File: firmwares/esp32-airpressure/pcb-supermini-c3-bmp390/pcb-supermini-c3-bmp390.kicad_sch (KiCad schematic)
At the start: 11 parts, among them J1 JST GH 4_Socket, U1 ESP32-C3_SUPERMINI_SMD, U2 BMP390 MODULE, U3 CAN transciever

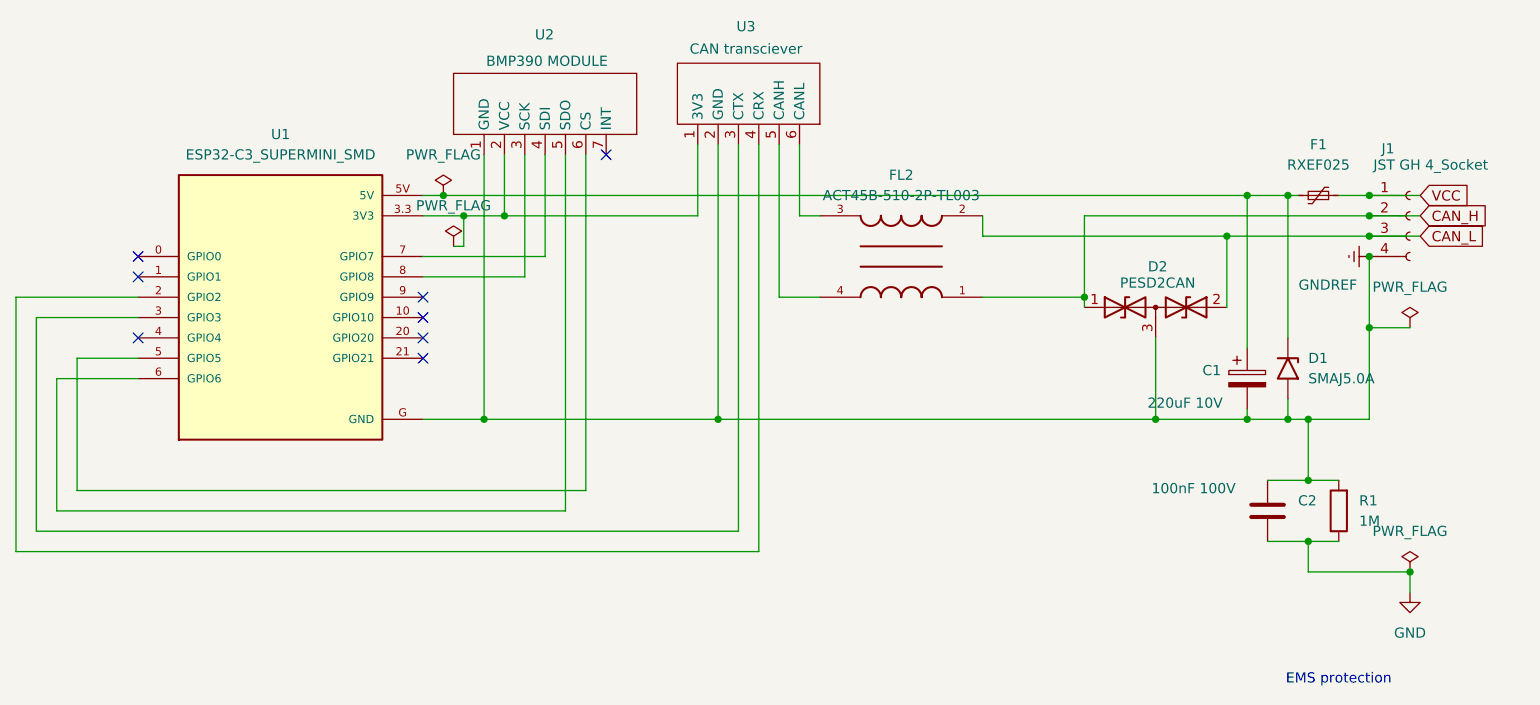
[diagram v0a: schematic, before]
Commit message: refactor: update PCB to be on 2 layers
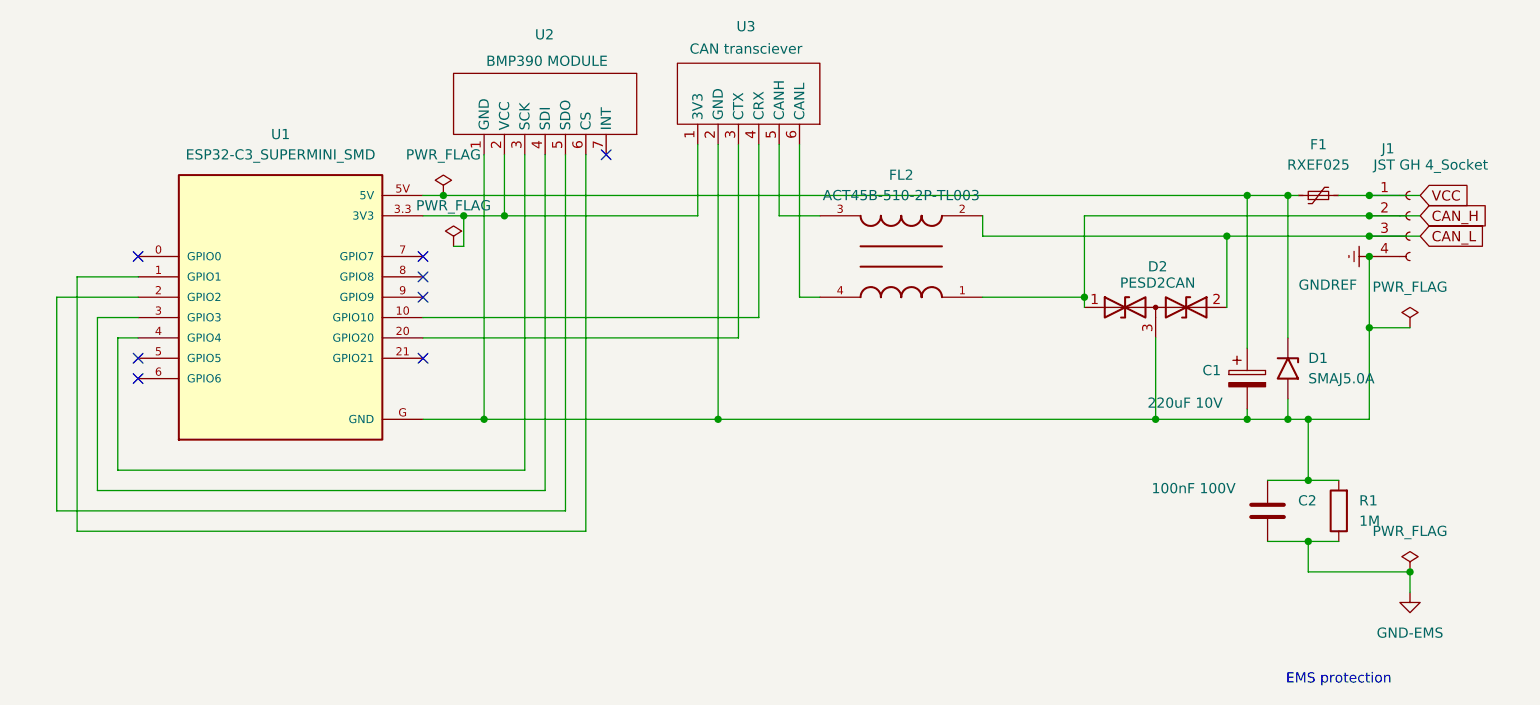
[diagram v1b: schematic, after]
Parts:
- J1: footprint Connector_JST:JST_GH_BM04B-GHS-TBT_1x04-1MP_P1.25mm_Vertical -> Connector_JST:JST_GH_SM04B-GHS-TB_1x04-1MP_P1.25mm_Horizontal
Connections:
- net at U1.1 (GPIO1): now also U2.6 (CS)
- net at U1.10 (GPIO10): now also U3.4 (CRX)
- net at U1.2 (GPIO2): now also U2.5 (SDO); no longer U3.4 (CRX)
- net at U1.20 (GPIO20): now also U3.3 (CTX)
- net at U1.3 (GPIO3): now also U2.4 (SDI); no longer U3.3 (CTX)
- net at U1.4 (GPIO4): now also U2.3 (SCK)
- net at U1.5 (GPIO5): no longer U2.6 (CS)
- net at U1.6 (GPIO6): no longer U2.5 (SDO)
- net at U1.7 (GPIO7): no longer U2.4 (SDI)
- net at U1.8 (GPIO8): no longer U2.3 (SCK)
- net at U3.5 (CANH): now also FL2.3; no longer FL2.4
- net at U3.6 (CANL): now also FL2.4; no longer FL2.3
- net GND renamed GND-EMS
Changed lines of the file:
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@@
 	)
 	(no_connect
-		(at 41.91 55.88)
+		(at 41.91 66.04)
 	)
 	(no_connect
-		(at 77.47 63.5)
+		(at 41.91 68.58)
 	)
 	(no_connect
-		(at 41.91 63.5)
+		(at 77.47 55.88)
 	)
 	(no_connect
-		(at 77.47 60.96)
+		(at 77.47 53.34)
 	)
 	(no_connect
@@
 	(wire
 		(pts
-			(xy 29.21 60.96) (xy 41.91 60.96)
-		)
-		(stroke
-			(width 0)
-			(type default)
-		)
-	)
-	(wire
-		(pts
 			(xy 114.3 39.37) (xy 114.3 73.66)
 		)
@@
 	(wire
 		(pts
-			(xy 34.29 82.55) (xy 97.79 82.55)
-		)
-		(stroke
-			(width 0)
-			(type default)
-		)
-	)
-	(wire
-		(pts
 			(xy 187.96 92.71) (xy 187.96 88.9)
 		)
@@
 	(wire
 		(pts
-			(xy 121.92 39.37) (xy 121.92 58.42)
-		)
-		(stroke
-			(width 0)
-			(type default)
-		)
-	)
-	(wire
-		(pts
 			(xy 85.09 73.66) (xy 77.47 73.66)
 		)
@@
 	(wire
 		(pts
-			(xy 119.38 39.37) (xy 119.38 90.17)
-		)
-		(stroke
-			(width 0)
-			(type default)
-		)
-	)
-	(wire
-		(pts
-			(xy 92.71 40.64) (xy 92.71 53.34)
+			(xy 116.84 63.5) (xy 116.84 39.37)
+		)
+		(stroke
+			(width 0)
+			(type default)
+		)
+	)
+	(wire
+		(pts
+			(xy 124.46 58.42) (xy 127 58.42)
 		)
 		(stroke
@@
 	(wire
 		(pts
-			(xy 127 48.26) (xy 124.46 48.26)
-		)
-		(stroke
-			(width 0)
-			(type default)
-		)
-	)
-	(wire
-		(pts
-			(xy 121.92 58.42) (xy 127 58.42)
-		)
-		(stroke
-			(width 0)
-			(type default)
-		)
-	)
-	(wire
-		(pts
 			(xy 185.42 71.12) (xy 185.42 73.66)
 		)
@@
 	(wire
 		(pts
-			(xy 31.75 85.09) (xy 31.75 68.58)
+			(xy 31.75 58.42) (xy 31.75 85.09)
 		)
 		(stroke
@@
 	(wire
 		(pts
-			(xy 97.79 82.55) (xy 97.79 40.64)
-		)
-		(stroke
-			(width 0)
-			(type default)
-		)
-	)
-	(wire
-		(pts
 			(xy 182.88 81.28) (xy 187.96 81.28)
 		)
@@
 	(wire
 		(pts
-			(xy 31.75 68.58) (xy 41.91 68.58)
+			(xy 36.83 82.55) (xy 36.83 60.96)
 		)
 		(stroke
@@
 	(wire
 		(pts
+			(xy 90.17 80.01) (xy 39.37 80.01)
+		)
+		(stroke
+			(width 0)
+			(type default)
+		)
+	)
+	(wire
+		(pts
 			(xy 95.25 40.64) (xy 95.25 85.09)
 		)
@@
 	(wire
 		(pts
-			(xy 34.29 66.04) (xy 34.29 82.55)
-		)
-		(stroke
-			(width 0)
-			(type default)
-		)
-	)
-	(wire
-		(pts
-			(xy 77.47 55.88) (xy 90.17 55.88)
+			(xy 39.37 80.01) (xy 39.37 63.5)
+		)
+		(stroke
+			(width 0)
+			(type default)
+		)
+	)
+	(wire
+		(pts
+			(xy 124.46 39.37) (xy 124.46 58.42)
+		)
+		(stroke
+			(width 0)
+			(type default)
+		)
+	)
+	(wire
+		(pts
+			(xy 121.92 39.37) (xy 121.92 48.26)
 		)
 		(stroke
@@
 	(wire
 		(pts
+			(xy 127 48.26) (xy 121.92 48.26)
+		)
+		(stroke
+			(width 0)
+			(type default)
+		)
+	)
+	(wire
+		(pts
 			(xy 195.58 73.66) (xy 187.96 73.66)
 		)
@@
 	(wire
 		(pts
-			(xy 41.91 66.04) (xy 34.29 66.04)
-		)
-		(stroke
-			(width 0)
-			(type default)
-		)
-	)
-	(wire
-		(pts
 			(xy 195.58 48.26) (xy 201.93 48.26)
 		)
@@
 	(wire
 		(pts
-			(xy 77.47 53.34) (xy 92.71 53.34)
-		)
-		(stroke
-			(width 0)
-			(type default)
-		)
-	)
-	(wire
-		(pts
-			(xy 119.38 90.17) (xy 26.67 90.17)
-		)
-		(stroke
-			(width 0)
-			(type default)
-		)
-	)
-	(wire
-		(pts
 			(xy 95.25 85.09) (xy 31.75 85.09)
 		)
@@
 	(wire
 		(pts
-			(xy 90.17 40.64) (xy 90.17 55.88)
-		)
-		(stroke
-			(width 0)
-			(type default)
-		)
-	)
-	(wire
-		(pts
 			(xy 80.01 45.72) (xy 180.34 45.72)
 		)
@@
 	(wire
 		(pts
+			(xy 36.83 60.96) (xy 41.91 60.96)
+		)
+		(stroke
+			(width 0)
+			(type default)
+		)
+	)
+	(wire
+		(pts
+			(xy 39.37 63.5) (xy 41.91 63.5)
+		)
+		(stroke
+			(width 0)
+			(type default)
+		)
+	)
+	(wire
+		(pts
 			(xy 160.02 48.26) (xy 160.02 58.42)
 		)
@@
 	(wire
 		(pts
-			(xy 26.67 90.17) (xy 26.67 58.42)
+			(xy 77.47 60.96) (xy 119.38 60.96)
+		)
+		(stroke
+			(width 0)
+			(type default)
+		)
+	)
+	(wire
+		(pts
+			(xy 92.71 40.64) (xy 92.71 82.55)
 		)
 		(stroke
@@
 	(wire
 		(pts
-			(xy 26.67 58.42) (xy 41.91 58.42)
-		)
-		(stroke
-			(width 0)
-			(type default)
-		)
-	)
-	(wire
-		(pts
 			(xy 111.76 39.37) (xy 111.76 48.26)
 		)
@@
 	(wire
 		(pts
+			(xy 97.79 40.64) (xy 97.79 87.63)
+		)
+		(stroke
+			(width 0)
+			(type default)
+		)
+	)
+	(wire
+		(pts
 			(xy 160.02 58.42) (xy 160.02 59.69)
 		)
@@
 	(wire
 		(pts
+			(xy 34.29 55.88) (xy 41.91 55.88)
+		)
+		(stroke
+			(width 0)
+			(type default)
+		)
+	)
+	(wire
+		(pts
 			(xy 187.96 81.28) (xy 191.77 81.28)
 		)
@@
 	(wire
 		(pts
+			(xy 90.17 40.64) (xy 90.17 80.01)
+		)
+		(stroke
+			(width 0)
+			(type default)
+		)
+	)
+	(wire
+		(pts
 			(xy 114.3 73.66) (xy 168.91 73.66)
 		)
@@
 	(wire
 		(pts
-			(xy 116.84 87.63) (xy 29.21 87.63)
+			(xy 77.47 63.5) (xy 116.84 63.5)
+		)
+		(stroke
+			(width 0)
+			(type default)
+		)
+	)
+	(wire
+		(pts
+			(xy 119.38 39.37) (xy 119.38 60.96)
+		)
+		(stroke
+			(width 0)
+			(type default)
+		)
+	)
+	(wire
+		(pts
+			(xy 41.91 58.42) (xy 31.75 58.42)
 		)
 		(stroke
@@
 	(wire
 		(pts
-			(xy 124.46 48.26) (xy 124.46 39.37)
+			(xy 34.29 87.63) (xy 34.29 55.88)
 		)
 		(stroke
@@
 	(wire
 		(pts
-			(xy 29.21 87.63) (xy 29.21 60.96)
-		)
-		(stroke
-			(width 0)
-			(type default)
-		)
-	)
-	(wire
-		(pts
 			(xy 195.58 53.34) (xy 195.58 62.23)
 		)
@@
 	(wire
 		(pts
+			(xy 92.71 82.55) (xy 36.83 82.55)
+		)
+		(stroke
+			(width 0)
+			(type default)
+		)
+	)
+	(wire
+		(pts
 			(xy 185.42 73.66) (xy 180.34 73.66)
 		)
@@
 	(wire
 		(pts
+			(xy 97.79 87.63) (xy 34.29 87.63)
+		)
+		(stroke
+			(width 0)
+			(type default)
+		)
+	)
+	(wire
+		(pts
 			(xy 180.34 72.39) (xy 180.34 73.66)
-		)
-		(stroke
-			(width 0)
-			(type default)
-		)
-	)
-	(wire
-		(pts
-			(xy 116.84 39.37) (xy 116.84 87.63)
 		)
 		(stroke
@@
 			)
 		)
-		(property "Value" "GND"
+		(property "Value" "GND-EMS"
 			(at 200.66 100.33 0)
 			(effects
@@
 			)
 		)
-		(property "Footprint" "Connector_JST:JST_GH_BM04B-GHS-TBT_1x04-1MP_P1.25mm_Vertical"
+		(property "Footprint" "Connector_JST:JST_GH_SM04B-GHS-TB_1x04-1MP_P1.25mm_Horizontal"
 			(at 200.66 48.26 0)
 			(effects
